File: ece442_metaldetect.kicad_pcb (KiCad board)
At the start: 2 copper layers, 81.3 x 25.4 mm, 42 parts, among them J1 1-2834011-2, J2 1-2834011-2, J3 Conn_01x03_Male, J4 Conn_01x08_Male, J5 Screw_Terminal_01x02, J6 Screw_Terminal_01x02, M1 Motor_DC, U1 LM1458N, U2 LMC6032IMX/NOPB, U3 LMC6032IMX/NOPB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

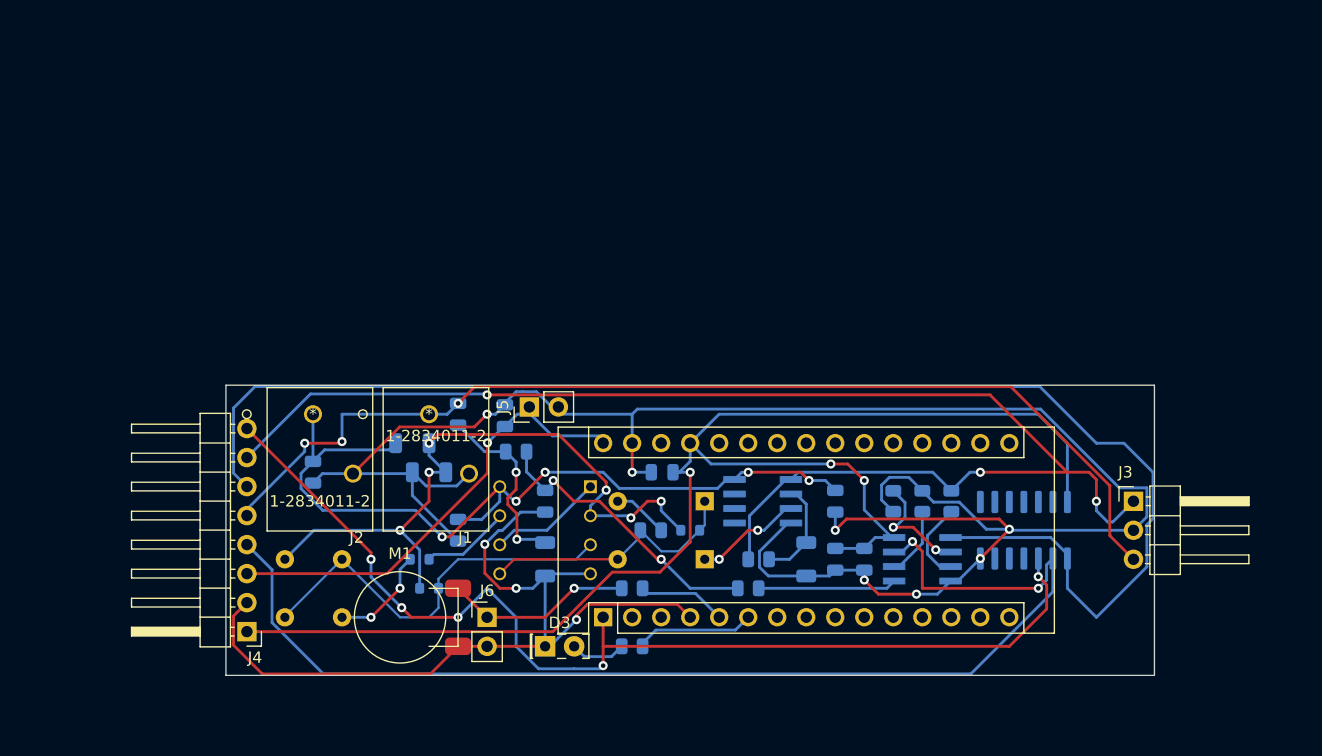
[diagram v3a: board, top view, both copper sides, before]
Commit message: shrunk width of board slightly, added ground pour and moved components
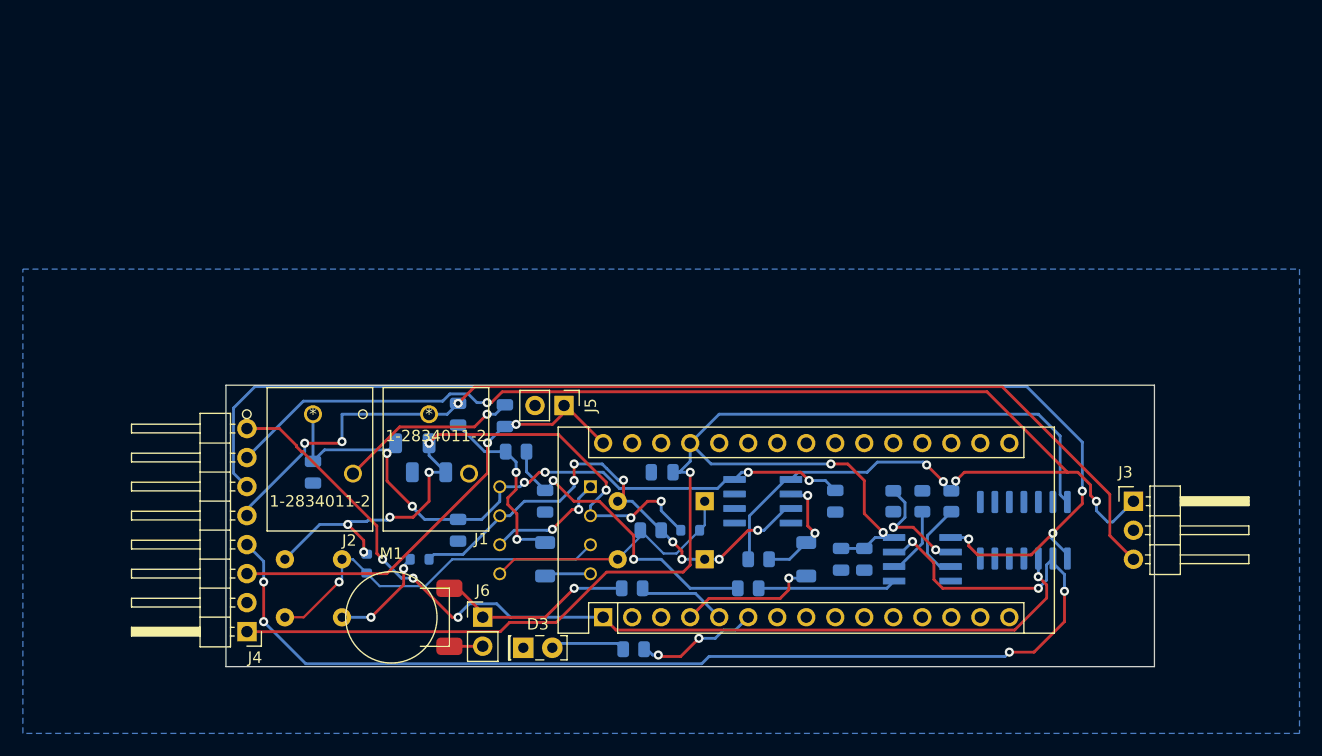
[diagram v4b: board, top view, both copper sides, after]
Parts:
- moved R6 5.87 mm to (93.6, 117.2), turned to 90 degrees
- moved J5 3.04 mm to (110.9, 103.4), turned to -90 degrees
- moved D3 1.91 mm to (107.3, 124.6)
- moved M1 0.76 mm to (95.8, 116.8)
- moved C9 0.51 mm to (135.1, 116.8)
- moved J6 0.38 mm to (103.8, 121.9)
- moved R16 0.28 mm to (117.0, 124.7)
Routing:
- net GND: track 259.8 -> 35.4 mm, vias 10 -> 2
- net /Sin1.4Vpp: track 22.1 -> 43.9 mm, vias 2 -> 7
- net /ReferenceSignalSquare: track 123.9 -> 107.1 mm, vias 0 -> 3
- net +12V: track 74.2 -> 60.6 mm, vias 5 -> 6
- net /PhaseShiftSquareWave: track 94.0 -> 84.8 mm, vias 5 -> 4
- net GNDREF: track 58.8 -> 56.0 mm, vias 6 -> 8
- net /OP1IN+2: track 35.1 -> 32.3 mm, vias 0 -> 1
- net Net-(D3-Pad2): track 4.91 -> 6.67 mm
- net /rxSignalSquare: track 103.6 -> 105.1 mm, vias 2 -> 6
- net +5V: track 121.9 -> 123.3 mm
- net /Sin12.0Vpp: track 121.5 -> 122.8 mm, vias 3 -> 5
- net Net-(C4-Pad2): track 25.3 -> 26.5 mm
- net /NegSigGenAmp: track 8.93 -> 10.1 mm, vias 0 -> 2
- net /OP1FB1: track 10.0 -> 10.6 mm, vias 0 -> 2
- net Net-(A1-Pad6): track 10.5 -> 10.9 mm, vias 0 -> 2
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- added copper zone on B.Cu, net GND
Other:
- board size 81.3 x 25.4 mm -> 81.3 x 24.6 mm

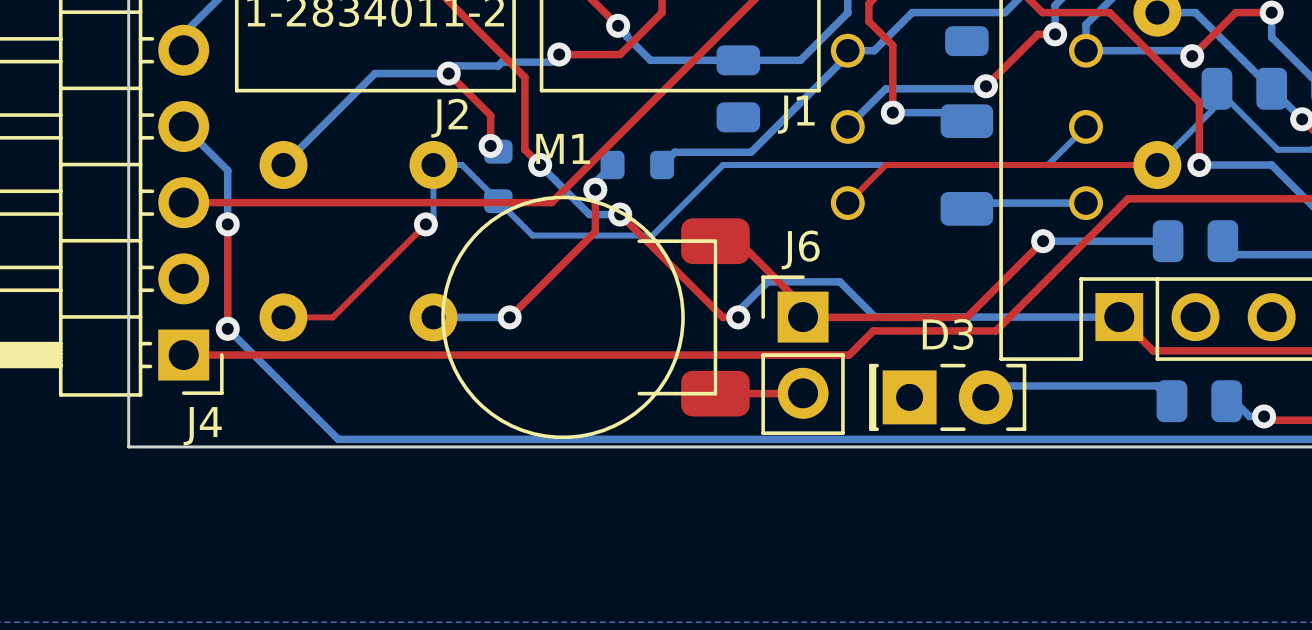
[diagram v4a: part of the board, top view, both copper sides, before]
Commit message: fixed clearance violation
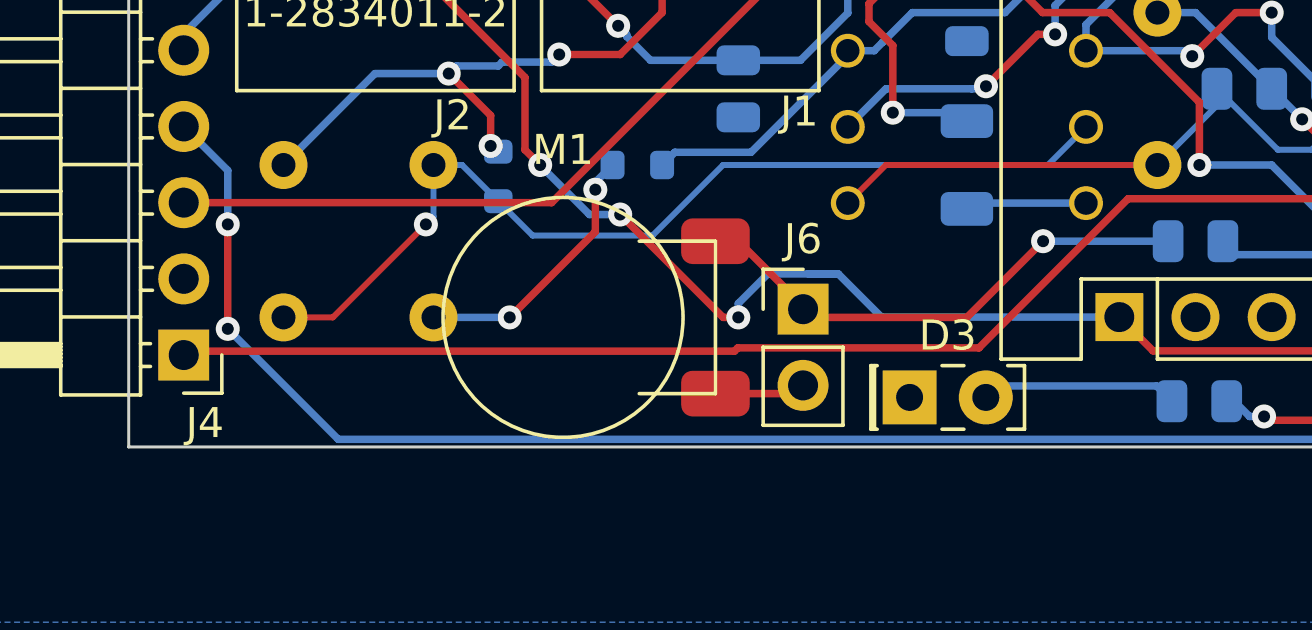
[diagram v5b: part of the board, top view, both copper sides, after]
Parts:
- moved J6 0.26 mm to (103.8, 121.6)
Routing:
- net /PhaseShiftSquareWave: track 84.8 -> 86.2 mm
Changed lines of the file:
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@@
   )
   (footprint "Connector_PinHeader_2.54mm:PinHeader_1x02_P2.54mm_Vertical" (layer "F.Cu")
-    (at 103.759 121.91)
+    (at 103.759 121.646)
     (descr "Through hole straight pin header, 1x02, 2.54mm pitch, single row")
     (tags "Through hole pin header THT 1x02 2.54mm single row")
@@
   (segment (start 96.637695 118.491) (end 97.663 118.491) (width 0.25) (layer "B.Cu") (net 1))
   (segment (start 94.996 116.84) (end 94.996 116.849305) (width 0.25) (layer "B.Cu") (net 1))
+  (segment (start 106.373 121.91) (end 104.934 120.471) (width 0.25) (layer "B.Cu") (net 1))
   (segment (start 152.4 118.355401) (end 152.387452 118.367949) (width 0.25) (layer "B.Cu") (net 1))
   (segment (start 94.996 116.849305) (end 96.637695 118.491) (width 0.25) (layer "B.Cu") (net 1))
-  (segment (start 102.584 120.735) (end 101.6 121.719) (width 0.25) (layer "B.Cu") (net 1))
-  (segment (start 101.6 121.719) (end 101.6 121.92) (width 0.25) (layer "B.Cu") (net 1))
-  (segment (start 114.3 121.91) (end 106.162 121.91) (width 0.25) (layer "B.Cu") (net 1))
-  (segment (start 106.162 121.91) (end 104.987 120.735) (width 0.25) (layer "B.Cu") (net 1))
-  (segment (start 104.987 120.735) (end 102.584 120.735) (width 0.25) (layer "B.Cu") (net 1))
+  (segment (start 101.6 121.455) (end 101.6 121.92) (width 0.25) (layer "B.Cu") (net 1))
+  (segment (start 102.584 120.471) (end 101.6 121.455) (width 0.25) (layer "B.Cu") (net 1))
+  (segment (start 104.934 120.471) (end 103.938 120.471) (width 0.25) (layer "B.Cu") (net 1))
+  (segment (start 114.3 121.91) (end 106.373 121.91) (width 0.25) (layer "B.Cu") (net 1))
   (segment (start 152.4 116.775) (end 152.4 118.355401) (width 0.25) (layer "B.Cu") (net 1))
+  (segment (start 104.934 120.471) (end 102.584 120.471) (width 0.25) (layer "B.Cu") (net 1))
   (segment (start 123.561 120.269) (end 129.794 120.269) (width 0.25) (layer "F.Cu") (net 4))
   (segment (start 104.14 124.46) (end 100.838 124.46) (width 0.25) (layer "F.Cu") (net 4))
@@
   (segment (start 124.1142 123.7595) (end 124.839189 123.034511) (width 0.25) (layer "B.Cu") (net 6))
   (segment (start 125.875489 123.034511) (end 127 121.91) (width 0.25) (layer "B.Cu") (net 6))
-  (segment (start 121.303489 117.964511) (end 121.92 117.348) (width 0.25) (layer "F.Cu") (net 27))
   (segment (start 137.16 109.9445) (end 137.16 112.841292) (width 0.25) (layer "F.Cu") (net 27))
+  (segment (start 109.622651 122.936) (end 114.59414 117.964511) (width 0.25) (layer "F.Cu") (net 27))
   (segment (start 137.16 112.841292) (end 138.810972 114.492264) (width 0.25) (layer "F.Cu") (net 27))
-  (segment (start 105.298 123.175) (end 106.103 122.37) (width 0.25) (layer "F.Cu") (net 27))
+  (segment (start 83.481 122.809) (end 83.717 123.045) (width 0.25) (layer "F.Cu") (net 27))
   (segment (start 121.92 117.348) (end 121.92 109.22) (width 0.25) (layer "F.Cu") (net 27))
-  (segment (start 106.103 122.37) (end 110.188651 122.37) (width 0.25) (layer "F.Cu") (net 27))
-  (segment (start 83.115 123.175) (end 105.298 123.175) (width 0.25) (layer "F.Cu") (net 27))
   (segment (start 114.59414 117.964511) (end 121.303489 117.964511) (width 0.25) (layer "F.Cu") (net 27))
-  (segment (start 110.188651 122.37) (end 114.59414 117.964511) (width 0.25) (layer "F.Cu") (net 27))
+  (segment (start 101.473 123.045) (end 101.582 122.936) (width 0.25) (layer "F.Cu") (net 27))
+  (segment (start 101.582 122.936) (end 109.622651 122.936) (width 0.25) (layer "F.Cu") (net 27))
+  (segment (start 83.115 123.175) (end 83.481 122.809) (width 0.25) (layer "F.Cu") (net 27))
+  (segment (start 83.717 123.045) (end 101.473 123.045) (width 0.25) (layer "F.Cu") (net 27))
   (segment (start 135.711 108.4955) (end 134.235342 108.4955) (width 0.25) (layer "F.Cu") (net 27))
   (segment (start 137.16 109.9445) (end 135.711 108.4955) (width 0.25) (layer "F.Cu") (net 27))
+  (segment (start 121.303489 117.964511) (end 121.92 117.348) (width 0.25) (layer "F.Cu") (net 27))
   (via (at 138.810972 114.492264) (size 0.8) (drill 0.4) (layers "F.Cu" "B.Cu") (net 27))
   (via (at 121.92 109.22) (size 0.8) (drill 0.4) (layers "F.Cu" "B.Cu") (net 27))

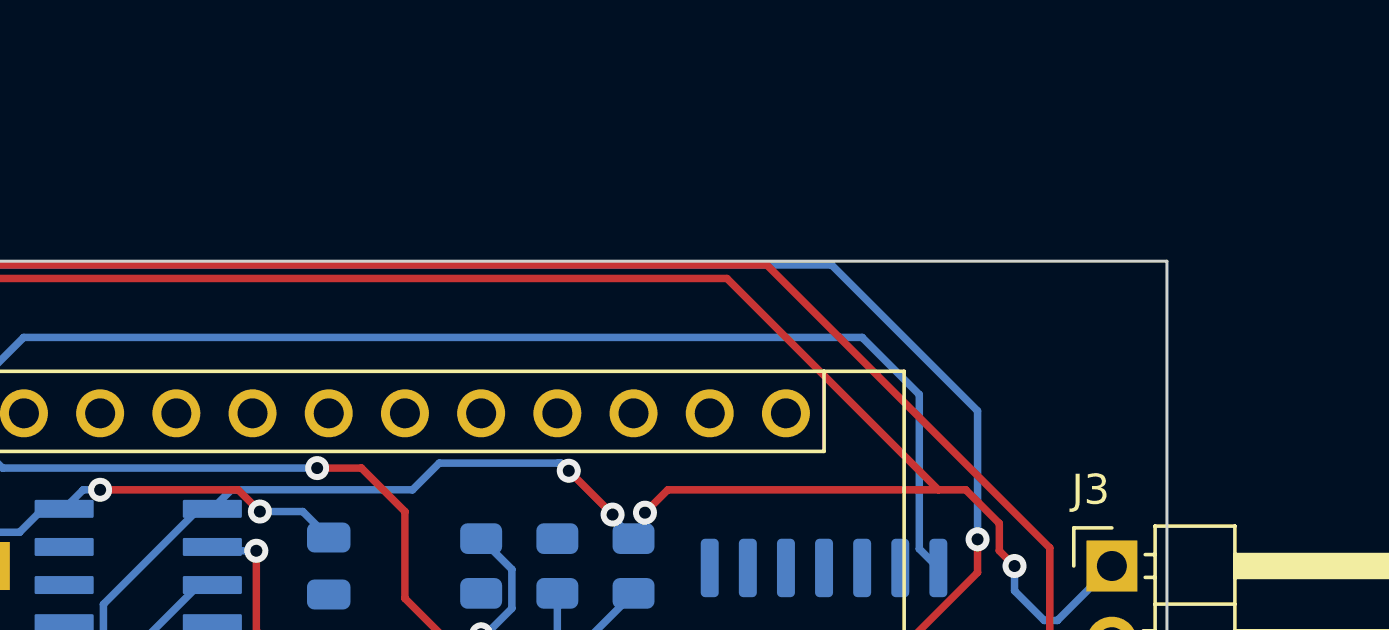
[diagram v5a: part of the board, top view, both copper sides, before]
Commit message: added silkscreen text showing version
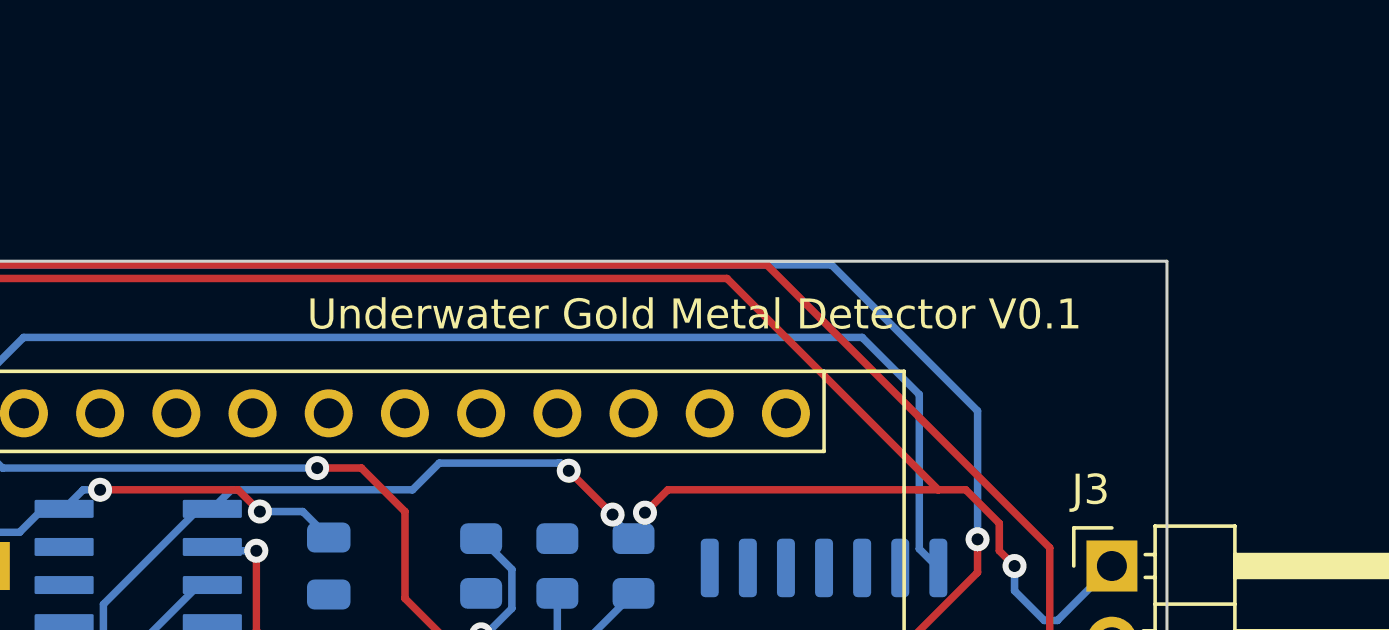
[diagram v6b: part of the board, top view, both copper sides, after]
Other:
- board text added: "Underwater Gold Metal Detector V0.1"
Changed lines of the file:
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@@
   )
   (gr_rect (start 162.56 126.238) (end 81.28 101.6) (layer "Edge.Cuts") (width 0.1) (fill none))
+  (gr_text "Underwater Gold Metal Detector V0.1" (at 146.812 103.378) (layer "F.SilkS")
+    (effects (font (size 1 1) (thickness 0.15)))
+  )
   (dimension (type aligned) (layer "F.Cu")
     (pts (xy 162.56 101.6) (xy 162.56 126.492))
